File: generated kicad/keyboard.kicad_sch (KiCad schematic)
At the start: 179 parts, among them J1 Conn_02x20_Top_Bottom, SW1 RotaryEncoder_Switch, SW2 RotaryEncoder_Switch

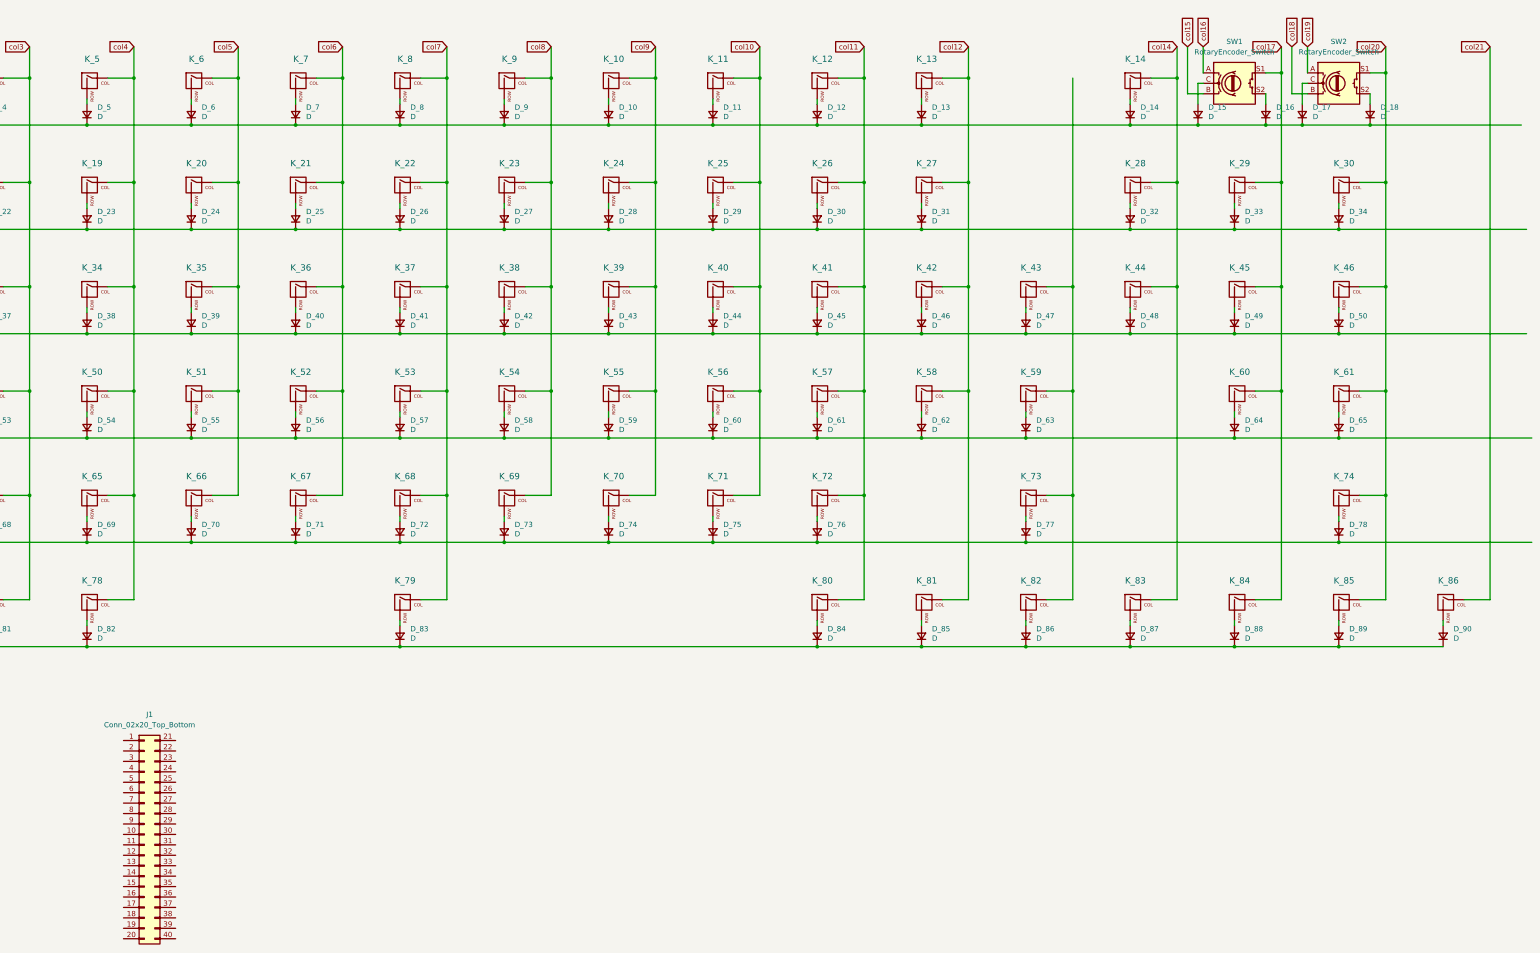
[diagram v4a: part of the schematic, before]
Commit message: stable but not enough pins
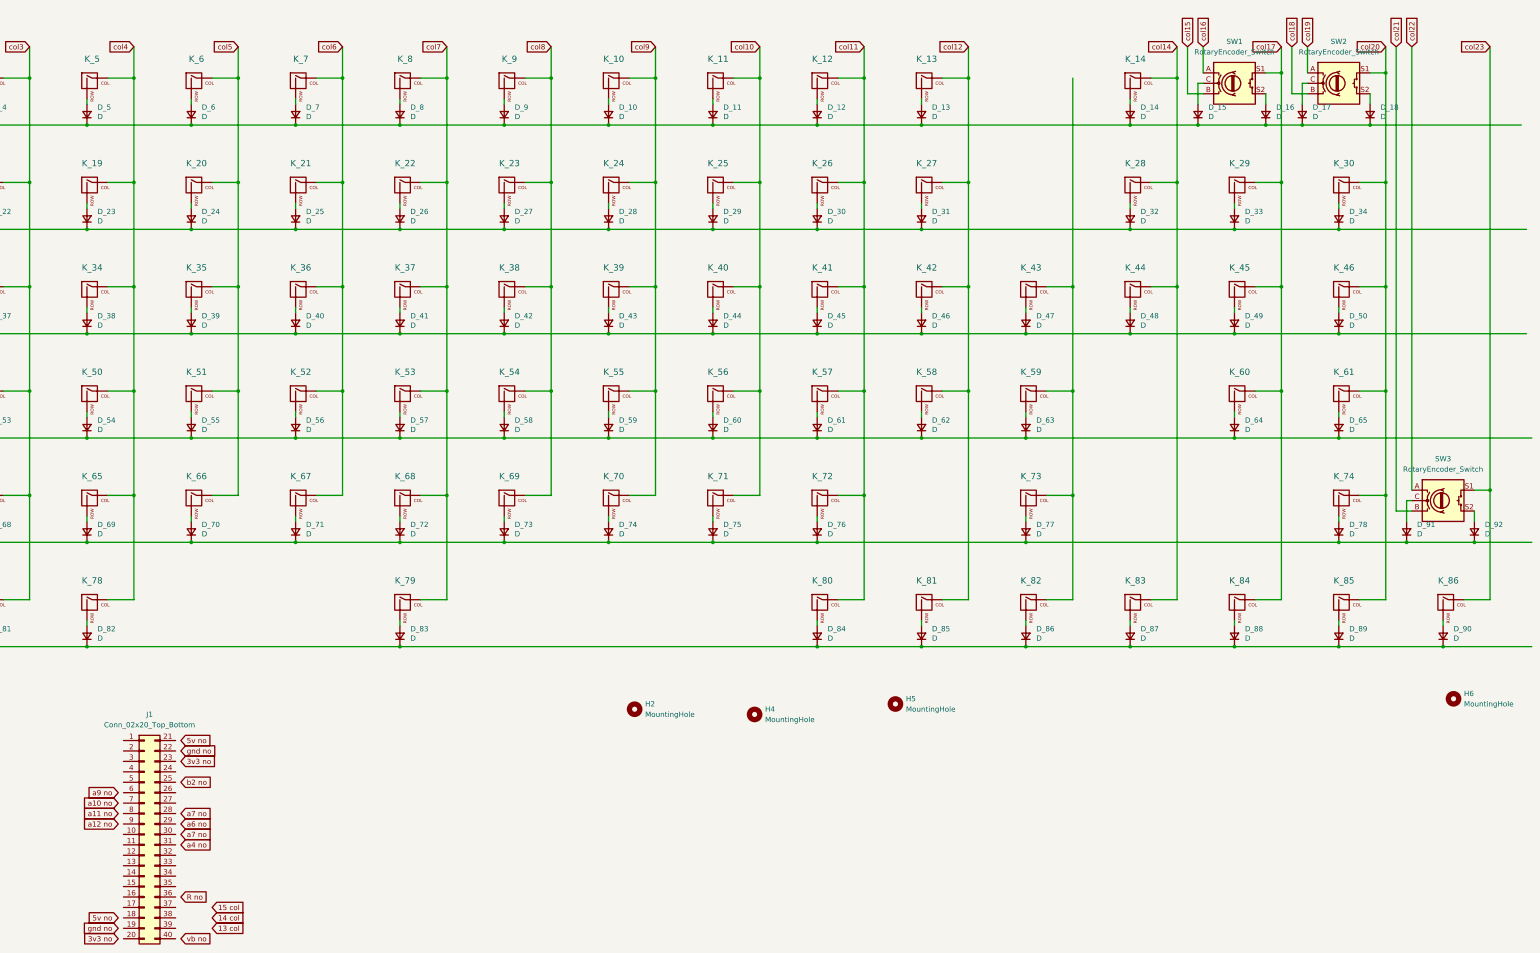
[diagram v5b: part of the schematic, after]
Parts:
- added D_91, D_92: D, Diode_SMD:D_SOD-123, symbol Device:D_Small
- added H2, H4, H5, H6: MountingHole, MountingHole:MountingHole_2.2mm_M2, symbol Mechanical:MountingHole
- added SW3: RotaryEncoder_Switch, Rotary_Encoder:RotaryEncoder_Alps_EC12E-Switch_Vertical_H20mm, symbol Device:RotaryEncoder_Switch
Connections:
- net col21: now also SW3.B; no longer K_86.1 (COL)
- net row4: now also D_91.1 (K), D_92.1 (K)
- new net: D_91.2 (A), SW3.C
- new net: D_92.2 (A), SW3.S2
- new net col22: SW3.A
- new net col23: K_86.1 (COL), SW3.S1

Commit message: need to flip pcb and fix footprint
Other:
- added sheet 12x8 (untitled.kicad_sch)
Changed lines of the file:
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@@
 		)
 	)
-	(global_label "a7 no"
-		(shape input)
-		(at 158.75 203.2 0)
-		(fields_autoplaced yes)
-		(effects
-			(font
-				(size 1.27 1.27)
-			)
-			(justify left)
-		)
-		(property "Intersheetrefs" "${INTERSHEET_REFS}"
-			(at 166.7051 203.2 0)
-			(effects
-				(font
-					(size 1.27 1.27)
-				)
-				(justify left)
-				(hide yes)
-			)
-		)
-	)
 	(global_label "col4"
 		(shape input)
@@
 		)
 	)
-	(global_label "a6 no"
-		(shape input)
-		(at 158.75 205.74 0)
-		(fields_autoplaced yes)
-		(effects
-			(font
-				(size 1.27 1.27)
-			)
-			(justify left)
-		)
-		(property "Intersheetrefs" "${INTERSHEET_REFS}"
-			(at 166.7051 205.74 0)
-			(effects
-				(font
-					(size 1.27 1.27)
-				)
-				(justify left)
-				(hide yes)
-			)
-		)
-	)
 	(global_label "5v no"
 		(shape input)
@@
 		)
 	)
-	(global_label "a7 no"
-		(shape input)
-		(at 158.75 208.28 0)
-		(fields_autoplaced yes)
-		(effects
-			(font
-				(size 1.27 1.27)
-			)
-			(justify left)
-		)
-		(property "Intersheetrefs" "${INTERSHEET_REFS}"
-			(at 166.7051 208.28 0)
-			(effects
-				(font
-					(size 1.27 1.27)
-				)
-				(justify left)
-				(hide yes)
-			)
-		)
-	)
 	(global_label "col2"
 		(shape input)
@@
 				)
 			)
+		)
+	)
+	(sheet
+		(at 564.515 357.505)
+		(size 12.7 13.335)
+		(fields_autoplaced yes)
+		(stroke
+			(width 0.1524)
+			(type solid)
+		)
+		(fill
+			(color 0 0 0 0.0000)
+		)
+		(property "Sheetname" "12x8"
+			(at 564.515 356.7934 0)
+			(effects
+				(font
+					(size 1.27 1.27)
+				)
+				(justify left bottom)
+			)
+		)
+		(property "Sheetfile" "untitled.kicad_sch"
+			(at 564.515 371.4246 0)
+			(effects
+				(font
+					(size 1.27 1.27)
+				)
+				(justify left top)
+			)
+		)
+		(instances
+			(project "keyboard"
+				(path "/4518914f-850f-4cd8-86f4-2792a0d788ad"
+					(page "2")
+				)
+			)

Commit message: fully done with fab no logo
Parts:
- removed H2, H4, H5, H6: MountingHole, MountingHole:MountingHole_2.2mm_M2, symbol Mechanical:MountingHole
